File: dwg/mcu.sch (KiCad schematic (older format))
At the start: 23 parts, among them J13 3221-10-0100-00, SW1 TL3342, U3 STM32F407VGTx, Y1 8MHz

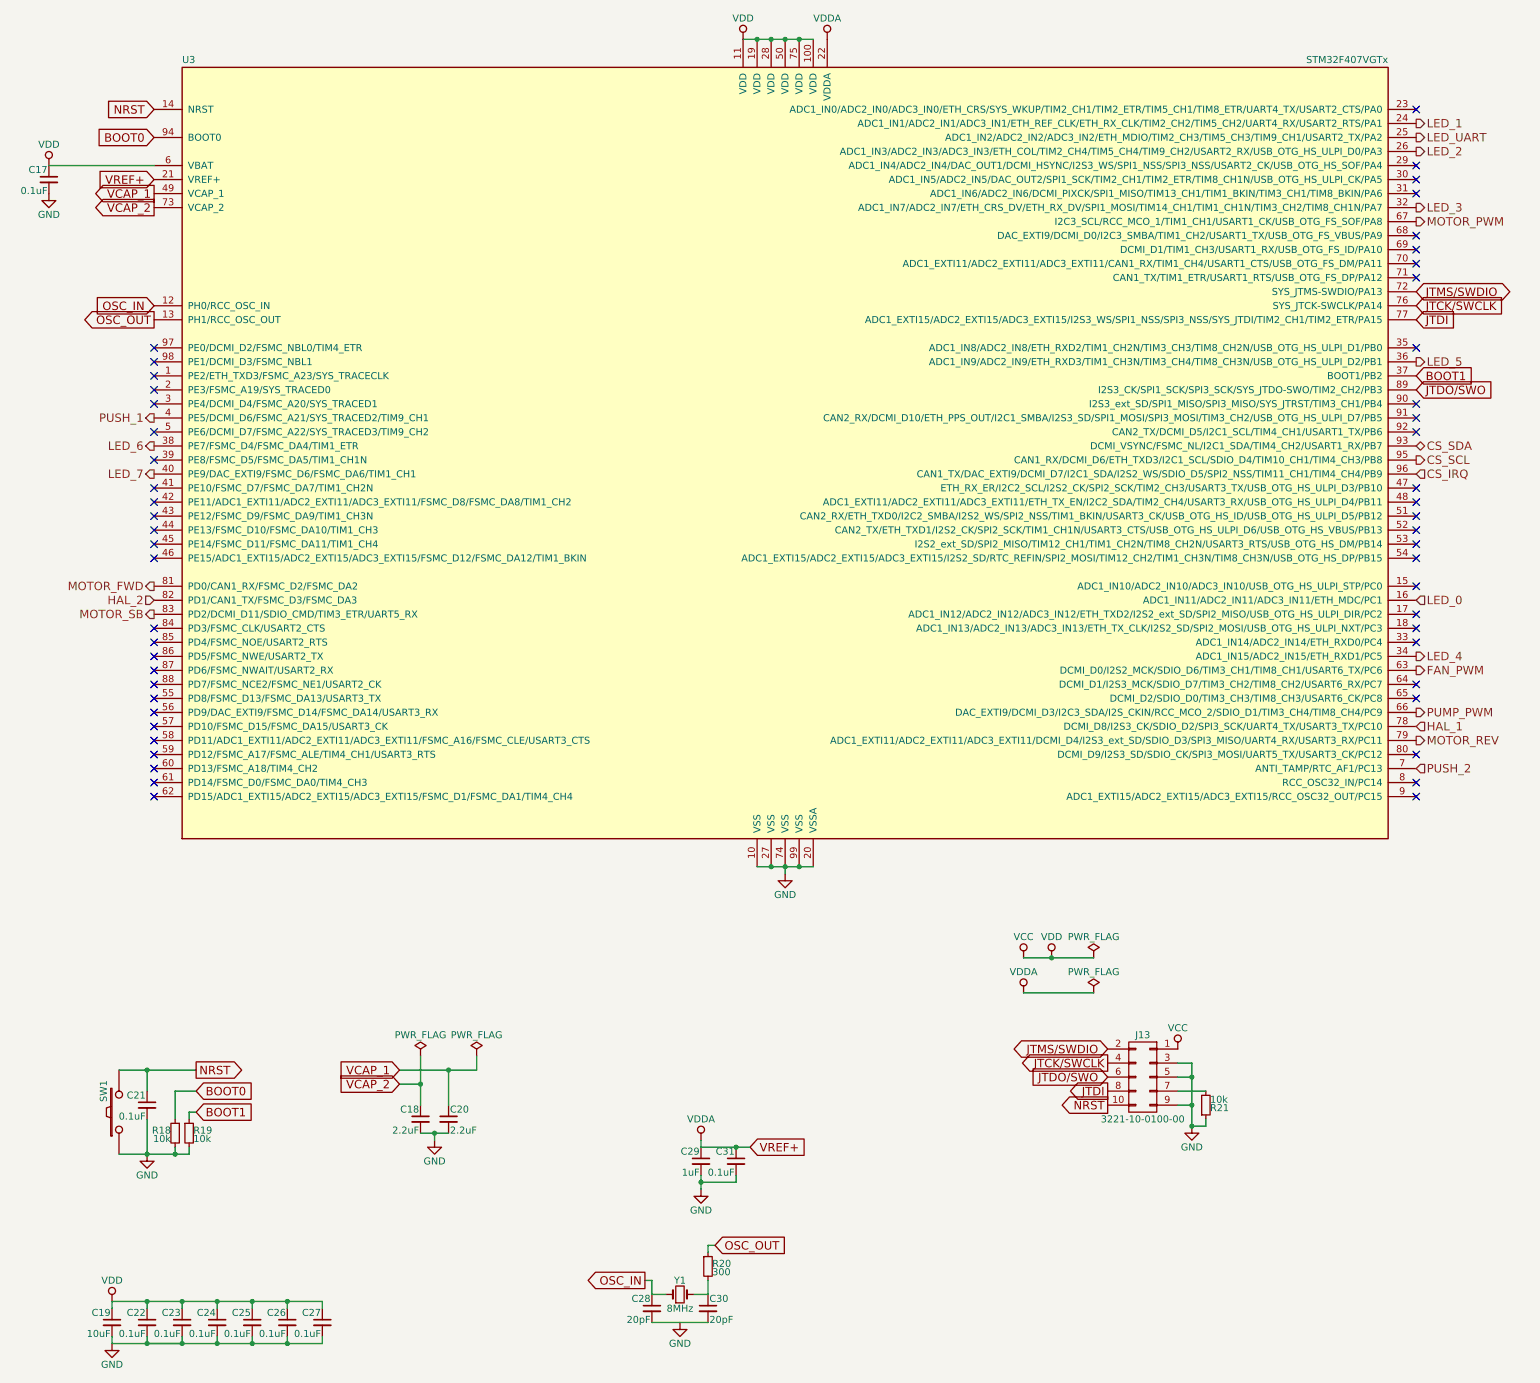
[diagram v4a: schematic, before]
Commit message: finished first round of routing. no drc errors
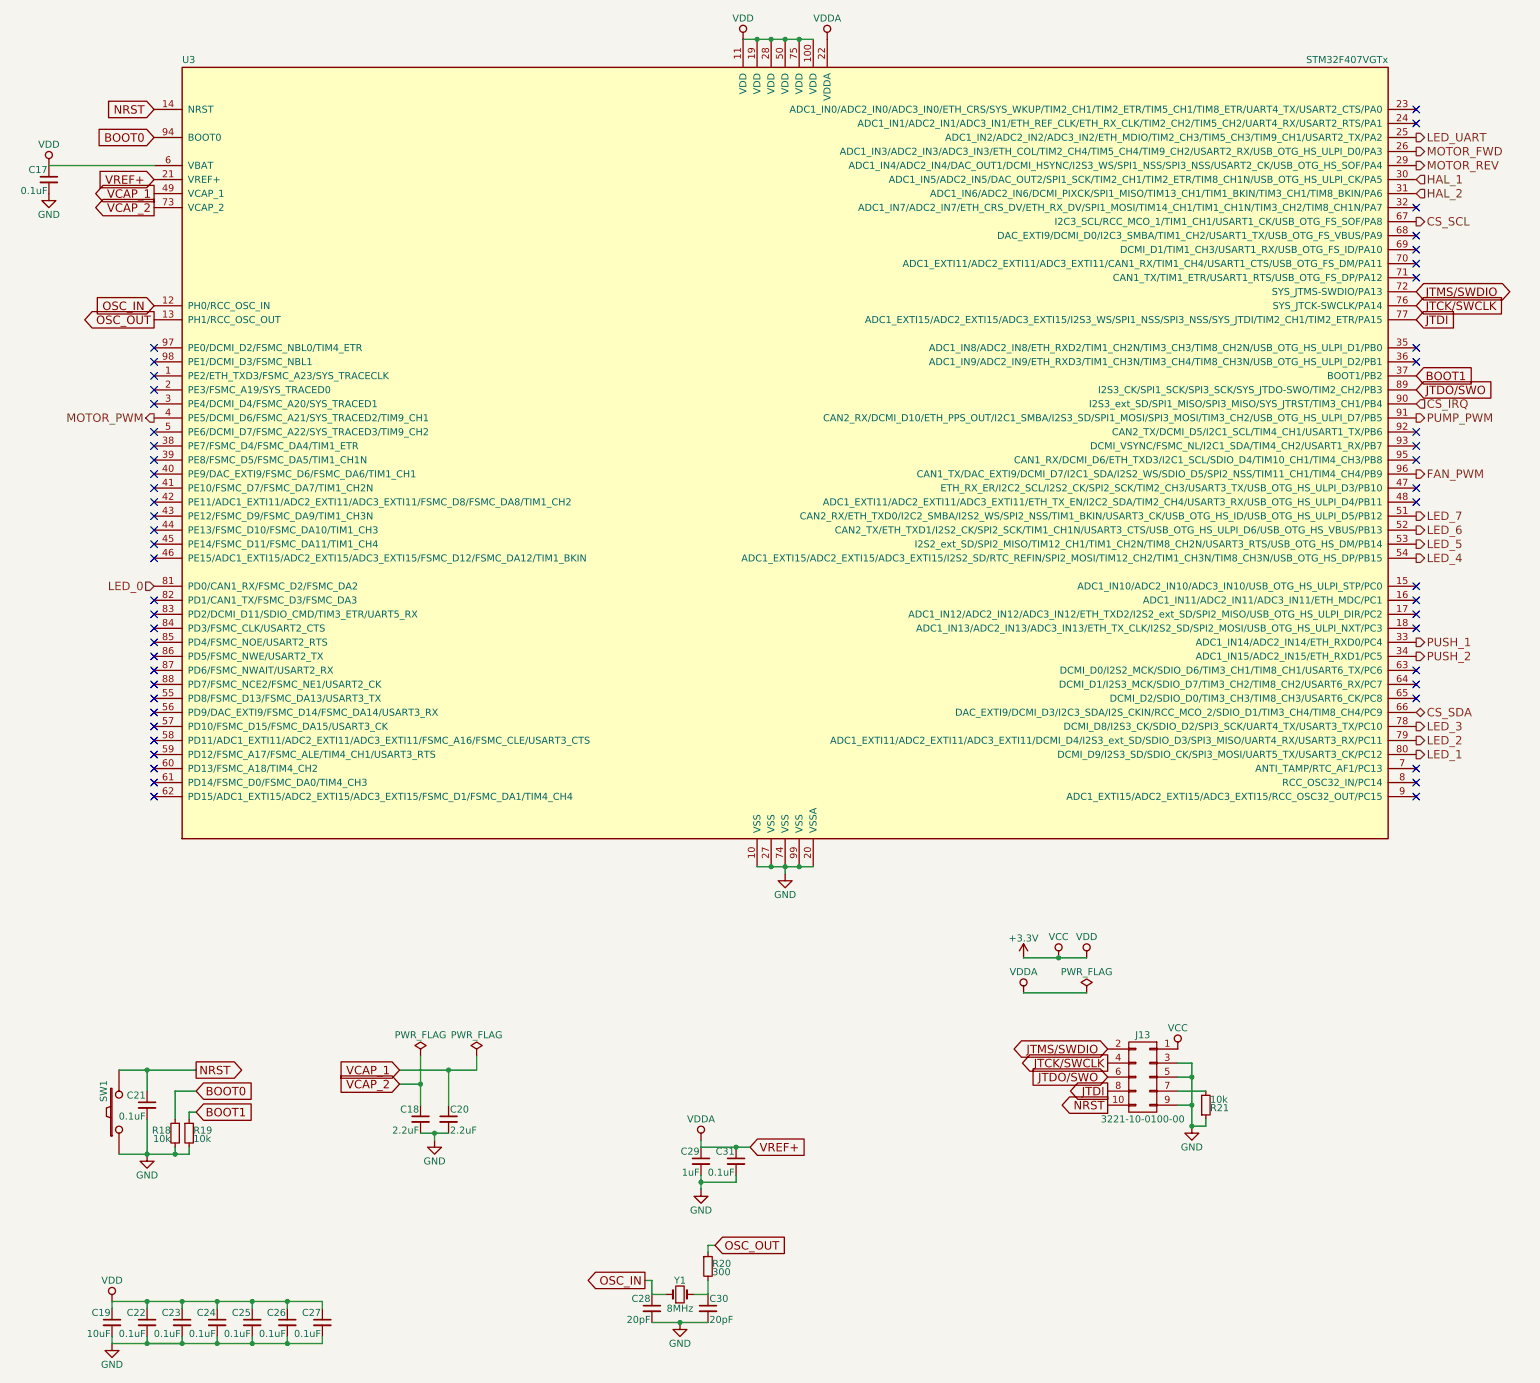
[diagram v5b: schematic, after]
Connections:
- net CS_IRQ: now also U3.90 (I2S3_ext_SD/SPI1_MISO/SPI3_MISO/SYS_JTRST/TIM3_CH1/PB4); no longer U3.96 (CAN1_TX/DAC_EXTI9/DCMI_D7/I2C1_SDA/I2S2_WS/SDIO_D5/SPI2_NSS/TIM11_CH1/TIM4_CH4/PB9)
- net CS_SCL: now also U3.67 (I2C3_SCL/RCC_MCO_1/TIM1_CH1/USART1_CK/USB_OTG_FS_SOF/PA8); no longer U3.95 (CAN1_RX/DCMI_D6/ETH_TXD3/I2C1_SCL/SDIO_D4/TIM10_CH1/TIM4_CH3/PB8)
- net CS_SDA: now also U3.66 (DAC_EXTI9/DCMI_D3/I2C3_SDA/I2S_CKIN/RCC_MCO_2/SDIO_D1/TIM3_CH4/TIM8_CH4/PC9); no longer U3.93 (DCMI_VSYNC/FSMC_NL/I2C1_SDA/TIM4_CH2/USART1_RX/PB7)
- net FAN_PWM: now also U3.96 (CAN1_TX/DAC_EXTI9/DCMI_D7/I2C1_SDA/I2S2_WS/SDIO_D5/SPI2_NSS/TIM11_CH1/TIM4_CH4/PB9); no longer U3.63 (DCMI_D0/I2S2_MCK/SDIO_D6/TIM3_CH1/TIM8_CH1/USART6_TX/PC6)
- net GND: now also C28.2, C30.2
- net HAL_1: now also U3.30 (ADC1_IN5/ADC2_IN5/DAC_OUT2/SPI1_SCK/TIM2_CH1/TIM2_ETR/TIM8_CH1N/USB_OTG_HS_ULPI_CK/PA5); no longer U3.78 (DCMI_D8/I2S3_CK/SDIO_D2/SPI3_SCK/UART4_TX/USART3_TX/PC10)
- net HAL_2: now also U3.31 (ADC1_IN6/ADC2_IN6/DCMI_PIXCK/SPI1_MISO/TIM13_CH1/TIM1_BKIN/TIM3_CH1/TIM8_BKIN/PA6); no longer U3.82 (PD1/CAN1_TX/FSMC_D3/FSMC_DA3)
- net LED_0: now also U3.81 (PD0/CAN1_RX/FSMC_D2/FSMC_DA2); no longer U3.16 (ADC1_IN11/ADC2_IN11/ADC3_IN11/ETH_MDC/PC1)
- net LED_1: now also U3.80 (DCMI_D9/I2S3_SD/SDIO_CK/SPI3_MOSI/UART5_TX/USART3_CK/PC12); no longer U3.24 (ADC1_IN1/ADC2_IN1/ADC3_IN1/ETH_REF_CLK/ETH_RX_CLK/TIM2_CH2/TIM5_CH2/UART4_RX/USART2_RTS/PA1)
- net LED_2: now also U3.79 (ADC1_EXTI11/ADC2_EXTI11/ADC3_EXTI11/DCMI_D4/I2S3_ext_SD/SDIO_D3/SPI3_MISO/UART4_RX/USART3_RX/PC11); no longer U3.26 (ADC1_IN3/ADC2_IN3/ADC3_IN3/ETH_COL/TIM2_CH4/TIM5_CH4/TIM9_CH2/USART2_RX/USB_OTG_HS_ULPI_D0/PA3)
- net LED_3: now also U3.78 (DCMI_D8/I2S3_CK/SDIO_D2/SPI3_SCK/UART4_TX/USART3_TX/PC10); no longer U3.32 (ADC1_IN7/ADC2_IN7/ETH_CRS_DV/ETH_RX_DV/SPI1_MOSI/TIM14_CH1/TIM1_CH1N/TIM3_CH2/TIM8_CH1N/PA7)
- net LED_4: now also U3.54 (ADC1_EXTI15/ADC2_EXTI15/ADC3_EXTI15/I2S2_SD/RTC_REFIN/SPI2_MOSI/TIM12_CH2/TIM1_CH3N/TIM8_CH3N/USB_OTG_HS_DP/PB15); no longer U3.34 (ADC1_IN15/ADC2_IN15/ETH_RXD1/PC5)
- net LED_5: now also U3.53 (I2S2_ext_SD/SPI2_MISO/TIM12_CH1/TIM1_CH2N/TIM8_CH2N/USART3_RTS/USB_OTG_HS_DM/PB14); no longer U3.36 (ADC1_IN9/ADC2_IN9/ETH_RXD3/TIM1_CH3N/TIM3_CH4/TIM8_CH3N/USB_OTG_HS_ULPI_D2/PB1)
- net LED_6: now also U3.52 (CAN2_TX/ETH_TXD1/I2S2_CK/SPI2_SCK/TIM1_CH1N/USART3_CTS/USB_OTG_HS_ULPI_D6/USB_OTG_HS_VBUS/PB13); no longer U3.38 (PE7/FSMC_D4/FSMC_DA4/TIM1_ETR)
- net LED_7: now also U3.51 (CAN2_RX/ETH_TXD0/I2C2_SMBA/I2S2_WS/SPI2_NSS/TIM1_BKIN/USART3_CK/USB_OTG_HS_ID/USB_OTG_HS_ULPI_D5/PB12); no longer U3.40 (PE9/DAC_EXTI9/FSMC_D6/FSMC_DA6/TIM1_CH1)
- net MOTOR_FWD: now also U3.26 (ADC1_IN3/ADC2_IN3/ADC3_IN3/ETH_COL/TIM2_CH4/TIM5_CH4/TIM9_CH2/USART2_RX/USB_OTG_HS_ULPI_D0/PA3); no longer U3.81 (PD0/CAN1_RX/FSMC_D2/FSMC_DA2)
- net MOTOR_PWM: now also U3.4 (PE5/DCMI_D6/FSMC_A21/SYS_TRACED2/TIM9_CH1); no longer U3.67 (I2C3_SCL/RCC_MCO_1/TIM1_CH1/USART1_CK/USB_OTG_FS_SOF/PA8)
- net MOTOR_REV: now also U3.29 (ADC1_IN4/ADC2_IN4/DAC_OUT1/DCMI_HSYNC/I2S3_WS/SPI1_NSS/SPI3_NSS/USART2_CK/USB_OTG_HS_SOF/PA4); no longer U3.79 (ADC1_EXTI11/ADC2_EXTI11/ADC3_EXTI11/DCMI_D4/I2S3_ext_SD/SDIO_D3/SPI3_MISO/UART4_RX/USART3_RX/PC11)
- net PUMP_PWM: now also U3.91 (CAN2_RX/DCMI_D10/ETH_PPS_OUT/I2C1_SMBA/I2S3_SD/SPI1_MOSI/SPI3_MOSI/TIM3_CH2/USB_OTG_HS_ULPI_D7/PB5); no longer U3.66 (DAC_EXTI9/DCMI_D3/I2C3_SDA/I2S_CKIN/RCC_MCO_2/SDIO_D1/TIM3_CH4/TIM8_CH4/PC9)
- net PUSH_1: now also U3.33 (ADC1_IN14/ADC2_IN14/ETH_RXD0/PC4); no longer U3.4 (PE5/DCMI_D6/FSMC_A21/SYS_TRACED2/TIM9_CH1)
- net PUSH_2: now also U3.34 (ADC1_IN15/ADC2_IN15/ETH_RXD1/PC5); no longer U3.7 (ANTI_TAMP/RTC_AF1/PC13)
- net MOTOR_SB: no longer names the net of U3.83 (PD2/DCMI_D11/SDIO_CMD/TIM3_ETR/UART5_RX)
- net VCC renamed +3V3
- no-connect marks 53 -> 54
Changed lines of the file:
@@
 	1    0    0    -1
 $EndComp
-Text HLabel 10450 4700 2    60   Input ~ 0
+Text HLabel 1450 4600 0    60   Input ~ 0
 LED_0
-Text HLabel 10450 1300 2    60   Output ~ 0
+Text HLabel 10450 5800 2    60   Output ~ 0
 LED_1
-Text HLabel 10450 1500 2    60   Output ~ 0
+Text HLabel 10450 5700 2    60   Output ~ 0
 LED_2
-Text HLabel 10450 1900 2    60   Output ~ 0
+Text HLabel 10450 5600 2    60   Output ~ 0
 LED_3
-Text HLabel 10450 5100 2    60   Output ~ 0
+Text HLabel 10450 4400 2    60   Output ~ 0
 LED_4
-Text HLabel 10450 3000 2    60   Output ~ 0
+Text HLabel 10450 4300 2    60   Output ~ 0
 LED_5
-Text HLabel 1450 3600 0    60   Output ~ 0
+Text HLabel 10450 4200 2    60   Output ~ 0
 LED_6
-Text HLabel 1450 3800 0    60   Output ~ 0
+Text HLabel 10450 4100 2    60   Output ~ 0
 LED_7
 Text HLabel 10450 1400 2    60   Output ~ 0
 LED_UART
-Text HLabel 10450 5600 2    60   Input ~ 0
+Text HLabel 10450 1700 2    60   Input ~ 0
 HAL_1
-Text HLabel 1450 4700 0    60   Input ~ 0
+Text HLabel 10450 1800 2    60   Input ~ 0
 HAL_2
+Text HLabel 10450 5000 2    60   Output ~ 0
+PUSH_1
+Text HLabel 10450 5100 2    60   Output ~ 0
+PUSH_2
+Text HLabel 10450 3300 2    60   Input ~ 0
+CS_IRQ
+Text HLabel 10450 2000 2    60   Output ~ 0
+CS_SCL
+Text HLabel 10450 5500 2    60   BiDi ~ 0
+CS_SDA
+Text HLabel 10450 1500 2    60   Output ~ 0
+MOTOR_FWD
+Text HLabel 10450 1600 2    60   Output ~ 0
+MOTOR_REV
 Text HLabel 1450 3400 0    60   Output ~ 0
-PUSH_1
-Text HLabel 10450 5900 2    60   Input ~ 0
-PUSH_2
-Text HLabel 10450 3800 2    60   Input ~ 0
-CS_IRQ
-Text HLabel 10450 3700 2    60   Output ~ 0
-CS_SCL
-Text HLabel 10450 3600 2    60   BiDi ~ 0
-CS_SDA
-Text HLabel 1450 4800 0    60   Output ~ 0
-MOTOR_SB
-Text HLabel 1450 4600 0    60   Output ~ 0
-MOTOR_FWD
-Text HLabel 10450 5700 2    60   Output ~ 0
-MOTOR_REV
-Text HLabel 10450 2000 2    60   Output ~ 0
 MOTOR_PWM
-Text HLabel 10450 5200 2    60   Output ~ 0
+Text HLabel 10450 3800 2    60   Output ~ 0
 FAN_PWM
-Text HLabel 10450 5500 2    60   Output ~ 0
+Text HLabel 10450 3400 2    60   Output ~ 0
 PUMP_PWM
 $Comp
@@
 $EndComp
 $Comp
-L GND #PWR055
+L GND #PWR057
 U 1 1 591EE235
 P 1400 8650
-F 0 "#PWR055" H 1400 8400 50  0001 C CNN
+F 0 "#PWR057" H 1400 8400 50  0001 C CNN
 F 1 "GND" H 1400 8500 50  0000 C CNN
 F 2 "" H 1400 8650 50  0001 C CNN
@@
 BOOT0
 $Comp
-L VDD #PWR056
+L VDD #PWR058
 U 1 1 591DB64B
 P 5650 700
-F 0 "#PWR056" H 5650 550 50  0001 C CNN
+F 0 "#PWR058" H 5650 550 50  0001 C CNN
 F 1 "VDD" H 5650 850 50  0000 C CNN
 F 2 "" H 5650 700 50  0001 C CNN
@@
 $EndComp
 $Comp
-L VDD #PWR057
+L VDD #PWR059
 U 1 1 591E1DAF
 P 1150 9700
-F 0 "#PWR057" H 1150 9550 50  0001 C CNN
+F 0 "#PWR059" H 1150 9550 50  0001 C CNN
 F 1 "VDD" H 1150 9850 50  0000 C CNN
 F 2 "" H 1150 9700 50  0001 C CNN
@@
 $EndComp
 $Comp
-L GND #PWR058
+L GND #PWR060
 U 1 1 591E4031
 P 1150 10000
-F 0 "#PWR058" H 1150 9750 50  0001 C CNN
+F 0 "#PWR060" H 1150 9750 50  0001 C CNN
 F 1 "GND" H 1150 9850 50  0000 C CNN
 F 2 "" H 1150 10000 50  0001 C CNN
@@
 $EndComp
 $Comp
-L GND #PWR059
+L GND #PWR061
 U 1 1 591E547E
 P 700 1800
-F 0 "#PWR059" H 700 1550 50  0001 C CNN
+F 0 "#PWR061" H 700 1550 50  0001 C CNN
 F 1 "GND" H 700 1650 50  0000 C CNN
 F 2 "" H 700 1800 50  0001 C CNN
@@
 $EndComp
 $Comp
-L VDD #PWR060
+L VDD #PWR062
 U 1 1 591E5827
 P 700 1600
-F 0 "#PWR060" H 700 1450 50  0001 C CNN
+F 0 "#PWR062" H 700 1450 50  0001 C CNN
 F 1 "VDD" H 700 1750 50  0000 C CNN
 F 2 "" H 700 1600 50  0001 C CNN
@@
 $EndComp
 $Comp
-L VDDA #PWR061
+L VDDA #PWR063
 U 1 1 591E60AA
 P 6250 700
-F 0 "#PWR061" H 6250 550 50  0001 C CNN
+F 0 "#PWR063" H 6250 550 50  0001 C CNN
 F 1 "VDDA" H 6250 850 50  0000 C CNN
 F 2 "" H 6250 700 50  0001 C CNN
@@
 $EndComp
 $Comp
-L VDDA #PWR062
+L VDDA #PWR064
 U 1 1 591E60E3
 P 5350 8550
-F 0 "#PWR062" H 5350 8400 50  0001 C CNN
+F 0 "#PWR064" H 5350 8400 50  0001 C CNN
 F 1 "VDDA" H 5350 8700 50  0000 C CNN
 F 2 "" H 5350 8550 50  0001 C CNN
@@
 $EndComp
 $Comp
-L GND #PWR063
+L GND #PWR065
 U 1 1 591E65D4
 P 5350 8900
-F 0 "#PWR063" H 5350 8650 50  0001 C CNN
+F 0 "#PWR065" H 5350 8650 50  0001 C CNN
 F 1 "GND" H 5350 8750 50  0000 C CNN
 F 2 "" H 5350 8900 50  0001 C CNN
@@
 VREF+
 $Comp
-L GND #PWR064
+L GND #PWR066
 U 1 1 591E7CD6
 P 5950 6650
-F 0 "#PWR064" H 5950 6400 50  0001 C CNN
+F 0 "#PWR066" H 5950 6400 50  0001 C CNN
 F 1 "GND" H 5950 6500 50  0000 C CNN
 F 2 "" H 5950 6650 50  0001 C CNN
@@
 $EndComp
 $Comp
-L GND #PWR065
+L GND #PWR067
 U 1 1 591E8ABB
 P 3450 8550
-F 0 "#PWR065" H 3450 8300 50  0001 C CNN
+F 0 "#PWR067" H 3450 8300 50  0001 C CNN
 F 1 "GND" H 3450 8400 50  0000 C CNN
 F 2 "" H 3450 8550 50  0001 C CNN
@@
 $EndComp
 $Comp
-L GND #PWR066
+L GND #PWR068
 U 1 1 5920CBAA
 P 5200 9850
-F 0 "#PWR066" H 5200 9600 50  0001 C CNN
+F 0 "#PWR068" H 5200 9600 50  0001 C CNN
 F 1 "GND" H 5200 9700 50  0000 C CNN
 F 2 "" H 5200 9850 50  0001 C CNN
@@
 	8950 8200 8750 8200
 $Comp
-L GND #PWR067
+L GND #PWR069
 U 1 1 592312DC
 P 8850 8450
-F 0 "#PWR067" H 8850 8200 50  0001 C CNN
+F 0 "#PWR069" H 8850 8200 50  0001 C CNN
 F 1 "GND" H 8850 8300 50  0000 C CNN
 F 2 "" H 8850 8450 50  0001 C CNN
@@
 $EndComp
 $Comp
-L VCC #PWR068
+L VCC #PWR070
 U 1 1 59231779
 P 8750 7900
-F 0 "#PWR068" H 8750 7750 50  0001 C CNN
+F 0 "#PWR070" H 8750 7750 50  0001 C CNN
 F 1 "VCC" H 8750 8050 50  0000 C CNN
 F 2 "" H 8750 7900 50  0001 C CNN
@@
 NoConn ~ 1450 3100
 NoConn ~ 1450 3200
-NoConn ~ 1450 3300
-NoConn ~ 1450 3500
 NoConn ~ 1450 3700
-NoConn ~ 10450 1200
-NoConn ~ 10450 1600
-NoConn ~ 10450 1700
-NoConn ~ 10450 1800
 NoConn ~ 10450 2100
 NoConn ~ 10450 2200
@@
 NoConn ~ 10450 3900
 NoConn ~ 10450 4000
-NoConn ~ 10450 4100
-NoConn ~ 10450 4200
-NoConn ~ 10450 4300
-NoConn ~ 10450 4400
-NoConn ~ 10450 3400
 NoConn ~ 10450 4600
 NoConn ~ 10450 4800
 NoConn ~ 10450 4900
-NoConn ~ 10450 5000
 NoConn ~ 10450 5300
 NoConn ~ 10450 5400
-NoConn ~ 10450 5800
 NoConn ~ 10450 6000
 NoConn ~ 10450 6100
 NoConn ~ 10450 2900
 NoConn ~ 10450 3500
-NoConn ~ 10450 3300
-$Comp
-L VCC #PWR069
+$Comp
+L VCC #PWR071
 U 1 1 592E53BB
-P 7650 7250
-F 0 "#PWR069" H 7650 7100 50  0001 C CNN
-F 1 "VCC" H 7650 7400 50  0000 C CNN
-F 2 "" H 7650 7250 50  0001 C CNN
-F 3 "" H 7650 7250 50  0001 C CNN
-	1    7650 7250
-	1    0    0    -1
-$EndComp
-$Comp
-L VDD #PWR070
+P 7900 7250
+F 0 "#PWR071" H 7900 7100 50  0001 C CNN
+F 1 "VCC" H 7900 7400 50  0000 C CNN
+F 2 "" H 7900 7250 50  0001 C CNN
+F 3 "" H 7900 7250 50  0001 C CNN
+	1    7900 7250
+	1    0    0    -1
+$EndComp
+$Comp
+L VDD #PWR072
 U 1 1 592E5592
-P 7850 7250
-F 0 "#PWR070" H 7850 7100 50  0001 C CNN
-F 1 "VDD" H 7850 7400 50  0000 C CNN
-F 2 "" H 7850 7250 50  0001 C CNN
-F 3 "" H 7850 7250 50  0001 C CNN
-	1    7850 7250
-	1    0    0    -1
-$EndComp
-$Comp
-L PWR_FLAG #FLG071
-U 1 1 592E58C4
-P 8150 7250
-F 0 "#FLG071" H 8150 7325 50  0001 C CNN
-F 1 "PWR_FLAG" H 8150 7400 50  0000 C CNN
-F 2 "" H 8150 7250 50  0001 C CNN
-F 3 "" H 8150 7250 50  0001 C CNN
-	1    8150 7250
-	1    0    0    -1
-$EndComp
-Wire Wire Line
-	7650 7250 8150 7250
-Connection ~ 7850 7250
-$Comp
-L VDDA #PWR072
+P 8100 7250
+F 0 "#PWR072" H 8100 7100 50  0001 C CNN
+F 1 "VDD" H 8100 7400 50  0000 C CNN
+F 2 "" H 8100 7250 50  0001 C CNN
+F 3 "" H 8100 7250 50  0001 C CNN
+	1    8100 7250
+	1    0    0    -1
+$EndComp
+$Comp
+L VDDA #PWR073
 U 1 1 592E663C
 P 7650 7500
-F 0 "#PWR072" H 7650 7350 50  0001 C CNN
+F 0 "#PWR073" H 7650 7350 50  0001 C CNN
 F 1 "VDDA" H 7650 7650 50  0000 C CNN
 F 2 "" H 7650 7500 50  0001 C CNN
@@
 	1    0    0    -1
 $EndComp
-$Comp
-L PWR_FLAG #FLG073
-U 1 1 592E6772
-P 8150 7500
-F 0 "#FLG073" H 8150 7575 50  0001 C CNN
-F 1 "PWR_FLAG" H 8150 7650 50  0000 C CNN
-F 2 "" H 8150 7500 50  0001 C CNN
-F 3 "" H 8150 7500 50  0001 C CNN
-	1    8150 7500
-	1    0    0    -1
-$EndComp
-Wire Wire Line
-	8150 7500 7650 7500
 Text GLabel 1450 1800 0    60   Output ~ 0
 VCAP_1
@@
 VCAP_2
 $Comp
-L PWR_FLAG #FLG074
+L PWR_FLAG #FLG075
 U 1 1 592E943D
 P 3350 7950
-F 0 "#FLG074" H 3350 8025 50  0001 C CNN
+F 0 "#FLG075" H 3350 8025 50  0001 C CNN
 F 1 "PWR_FLAG" H 3350 8100 50  0000 C CNN
 F 2 "" H 3350 7950 50  0001 C CNN
@@
 $EndComp
 $Comp
-L PWR_FLAG #FLG075
+L PWR_FLAG #FLG076
 U 1 1 592E98C6
 P 3750 7950
-F 0 "#FLG075" H 3750 8025 50  0001 C CNN
+F 0 "#FLG076" H 3750 8025 50  0001 C CNN
 F 1 "PWR_FLAG" H 3750 8100 50  0000 C CNN
 F 2 "" H 3750 7950 50  0001 C CNN
@@
 	3750 8050 3750 7950
 Connection ~ 3550 8050
+NoConn ~ 10450 1900
+$Comp
+L +3.3V #PWR077
+U 1 1 5934B114
+P 7650 7250
+F 0 "#PWR077" H 7650 7100 50  0001 C CNN
+F 1 "+3.3V" H 7650 7390 50  0000 C CNN
+F 2 "" H 7650 7250 50  0001 C CNN
+F 3 "" H 7650 7250 50  0001 C CNN
+	1    7650 7250
+	1    0    0    -1
+$EndComp
+Connection ~ 7900 7250
+Connection ~ 5200 9850
+NoConn ~ 1450 3300
+NoConn ~ 1450 3500
+NoConn ~ 1450 3600
+NoConn ~ 1450 3800
+NoConn ~ 1450 4800
+NoConn ~ 1450 4700
+NoConn ~ 10450 5900
+NoConn ~ 10450 5200
+NoConn ~ 10450 4700
+NoConn ~ 10450 3700
+NoConn ~ 10450 3600
+NoConn ~ 10450 3000
+NoConn ~ 10450 1300
+NoConn ~ 10450 1200
+Wire Wire Line
+	7650 7250 8100 7250
+$Comp
+L PWR_FLAG #FLG074
+U 1 1 592E6772
+P 8100 7500
+F 0 "#FLG074" H 8100 7575 50  0001 C CNN
+F 1 "PWR_FLAG" H 8100 7650 50  0000 C CNN
+F 2 "" H 8100 7500 50  0001 C CNN
+F 3 "" H 8100 7500 50  0001 C CNN
+	1    8100 7500
+	1    0    0    -1
+$EndComp
+Wire Wire Line
+	8100 7500 7650 7500
 $EndSCHEMATC
